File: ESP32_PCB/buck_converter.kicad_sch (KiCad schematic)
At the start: 8 parts, among them U4 TPS54302

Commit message: start pcb
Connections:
- net GNDREF: now also C10.1
- net at C9.1, R7.2, R8.1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: no longer C10.1
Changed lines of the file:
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@@
+		(color 0 0 0 0)
+	)
+	(junction
+		(at 187.96 80.01)
+		(diameter 0)
 		(color 0 0 0 0)
 	)
@@
 	(wire
 		(pts
-			(xy 167.64 66.04) (xy 165.1 66.04)
+			(xy 198.12 72.39) (xy 198.12 80.01)
 		)
 		(stroke
@@
 	(wire
 		(pts
-			(xy 187.96 73.66) (xy 198.12 73.66)
+			(xy 167.64 66.04) (xy 165.1 66.04)
 		)
 		(stroke
@@
 	(wire
 		(pts
-			(xy 198.12 72.39) (xy 198.12 73.66)
+			(xy 198.12 80.01) (xy 187.96 80.01)
 		)
 		(stroke

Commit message: rerouting
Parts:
- C7: value 22uF -> 4.7uF
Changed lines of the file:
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@@
 			)
 		)
-		(property "Value" "22uF"
+		(property "Value" "4.7uF"
 			(at 138.43 59.8169 0)
 			(effects

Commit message: add lcsc pn
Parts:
- removed C7: 4.7uF, Capacitor_SMD:C_0603_1608Metric, symbol Device:C_Small_US
- added C3: 6.8uF, Capacitor_Tantalum_SMD:CP_EIA-3216-18_Kemet-A, symbol Device:C_Polarized_Small_US
- C10: footprint Capacitor_SMD:C_0402_1005Metric -> Capacitor_SMD:C_0805_2012Metric; LCSC PN (none) -> C16780
- C8: LCSC PN (none) -> C14663
- C9: value 56pF -> 82pF; LCSC PN (none) -> C1683
- L1: value 6.8uH -> 10uH; LCSC C207831 -> (none); LCSC PN (none) -> C207831
- R7: footprint Resistor_SMD:R_0603_1608Metric -> Resistor_SMD:R_0805_2012Metric; LCSC PN (none) -> C7319379
- R8: value 22k -> 13.7; footprint Resistor_SMD:R_0603_1608Metric -> Resistor_SMD:R_0805_2012Metric; LCSC PN (none) -> C409962
- U4: footprint Package_TO_SOT_SMD:SOT-23-6 -> Package_TO_SOT_SMD:SOT-563; LCSC PN (none) -> C50310967
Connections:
- net GNDREF: now also C3.2
- net VBATT: now also C3.1
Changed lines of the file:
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@@
+			)
+		)
+		(property "LCSC PN" "C14663"
+			(at 162.56 64.77 90)
+			(effects
+				(font
+					(size 1.27 1.27)
+				)
+				(hide yes)
+			)
+		)
+		(property "LCSC" ""
+			(at 162.56 64.77 90)
+			(effects
+				(font
+					(size 1.27 1.27)
+				)
+				(hide yes)
 			)
 		)
@@
 			)
 		)
-		(property "Footprint" "Package_TO_SOT_SMD:SOT-23-6"
+		(property "Footprint" "Package_TO_SOT_SMD:SOT-563"
 			(at 149.86 76.2 0)
 			(effects
@@
 		)
 		(property "Description" "3A, 4.5 to 28V Input, EMI Friendly integrated switch synchronous step-down regulator, pulse-skipping, SOT-23-6"
+			(at 148.59 67.31 0)
+			(effects
+				(font
+					(size 1.27 1.27)
+				)
+				(hide yes)
+			)
+		)
+		(property "LCSC PN" "C50310967"
+			(at 148.59 67.31 0)
+			(effects
+				(font
+					(size 1.27 1.27)
+				)
+				(hide yes)
+			)
+		)
+		(property "LCSC" ""
 			(at 148.59 67.31 0)
 			(effects
@@
 			)
 		)
-		(property "Footprint" "Capacitor_SMD:C_0402_1005Metric"
+		(property "Footprint" "Capacitor_SMD:C_0805_2012Metric"
 			(at 198.12 69.85 0)
 			(effects
@@
 		)
 		(property "Description" "capacitor, small US symbol"
+			(at 198.12 69.85 0)
+			(effects
+				(font
+					(size 1.27 1.27)
+				)
+				(hide yes)
+			)
+		)
+		(property "LCSC PN" "C16780"
+			(at 198.12 69.85 0)
+			(effects
+				(font
+					(size 1.27 1.27)
+				)
+				(hide yes)
+			)
+		)
+		(property "LCSC" ""
 			(at 198.12 69.85 0)
 			(effects
@@
 	(symbol
 		(lib_id "Device:C_Small_US")
-		(at 135.89 58.42 0)
-		(unit 1)
-		(exclude_from_sim no)
-		(in_bom yes)
-		(on_board yes)
-		(dnp no)
-		(fields_autoplaced yes)
-		(property "Reference" "C7"
-			(at 138.43 57.2769 0)
-			(effects
-				(font
-					(size 1.27 1.27)
-				)
-				(justify left)
-			)
-		)
-		(property "Value" "4.7uF"
-			(at 138.43 59.8169 0)
-			(effects
-				(font
-					(size 1.27 1.27)
-				)
-				(justify left)
-			)
-		)
-		(property "Footprint" "Capacitor_SMD:C_0603_1608Metric"
-			(at 135.89 58.42 0)
-			(effects
-				(font
-					(size 1.27 1.27)
-				)
-				(hide yes)
-			)
-		)
-		(property "Datasheet" ""
-			(at 135.89 58.42 0)
-			(effects
-				(font
-					(size 1.27 1.27)
-				)
-				(hide yes)
-			)
-		)
-		(property "Description" "capacitor, small US symbol"
-			(at 135.89 58.42 0)
-			(effects
-				(font
-					(size 1.27 1.27)
-				)
-				(hide yes)
-			)
-		)
-		(pin "1"
-		)
-		(pin "2"
-		)
-		(instances
-			(project ""
-				(path "/c820eee0-9a51-4601-b23c-3906ac354886/7478e98e-de6a-4a00-aa38-12c004b4cc7e"
-					(reference "C7")
-					(unit 1)
-				)
-			)
-		)
-	)
-	(symbol
-		(lib_id "Device:C_Small_US")
 		(at 177.8 69.85 180)
 		(unit 1)
@@
 			)
 		)
-		(property "Value" "56pF"
+		(property "Value" "82pF"
 			(at 180.34 70.9929 0)
 			(effects
@@
 		)
 		(property "Description" "capacitor, small US symbol"
+			(at 177.8 69.85 0)
+			(effects
+				(font
+					(size 1.27 1.27)
+				)
+				(hide yes)
+			)
+		)
+		(property "LCSC PN" "C1683"
+			(at 177.8 69.85 0)
+			(effects
+				(font
+					(size 1.27 1.27)
+				)
+				(hide yes)
+			)
+		)
+		(property "LCSC" ""
 			(at 177.8 69.85 0)
 			(effects
@@
 			)
 		)
-		(property "Value" "6.8uH"
+		(property "Value" "10uH"
 			(at 171.45 63.5 90)
 			(effects
@@
 			)
 		)
-		(property "LCSC" "C207831"
+		(property "LCSC PN" "C207831"
+			(at 171.45 66.04 90)
+			(effects
+				(font
+					(size 1.27 1.27)
+				)
+				(hide yes)
+			)
+		)
+		(property "LCSC" ""
 			(at 171.45 66.04 90)
 			(effects
@@
 	)
 	(symbol
+		(lib_id "Device:C_Polarized_Small_US")
+		(at 135.89 58.42 0)
+		(mirror x)
+		(unit 1)
+		(exclude_from_sim no)
+		(in_bom yes)
+		(on_board yes)
+		(dnp no)
+		(property "Reference" "C3"
+			(at 138.43 60.1219 0)
+			(effects
+				(font
+					(size 1.27 1.27)
+				)
+				(justify left)
+			)
+		)
+		(property "Value" "6.8uF"
+			(at 138.43 57.5819 0)
+			(effects
+				(font
+					(size 1.27 1.27)
+				)
+				(justify left)
+			)
+		)
+		(property "Footprint" "Capacitor_Tantalum_SMD:CP_EIA-3216-18_Kemet-A"
+			(at 135.89 58.42 0)
+			(effects
+				(font
+					(size 1.27 1.27)
+				)
+				(hide yes)
+			)
+		)
+		(property "Datasheet" "~"
+			(at 135.89 58.42 0)
+			(effects
+				(font
+					(size 1.27 1.27)
+				)
+				(hide yes)
+			)
+		)
+		(property "Description" "Polarized capacitor, small US symbol"
+			(at 135.89 58.42 0)
+			(effects
+				(font
+					(size 1.27 1.27)
+				)
+				(hide yes)
+			)
+		)
+		(property "LCSC PN" "C444749"
+			(at 135.89 58.42 0)
+			(effects
+				(font
+					(size 1.27 1.27)
+				)
+				(hide yes)
+			)
+		)
+		(property "LCSC" ""
+			(at 135.89 58.42 0)
+			(effects
+				(font
+					(size 1.27 1.27)
+				)
+				(hide yes)
+			)
+		)
+		(pin "1"
+		)
+		(pin "2"
+		)
+		(instances
+			(project ""
+				(path "/c820eee0-9a51-4601-b23c-3906ac354886/7478e98e-de6a-4a00-aa38-12c004b4cc7e"
+					(reference "C3")
+					(unit 1)
+				)
+			)
+		)
+	)
+	(symbol
 		(lib_id "Device:R_Small_US")
 		(at 187.96 77.47 0)
@@
 			)
 		)
-		(property "Value" "22k"
+		(property "Value" "13.7"
 			(at 190.5 78.7399 0)
 			(effects
@@
 			)
 		)
-		(property "Footprint" "Resistor_SMD:R_0603_1608Metric"
+		(property "Footprint" "Resistor_SMD:R_0805_2012Metric"
 			(at 187.96 77.47 0)
 			(effects
@@
 		)
 		(property "Description" "Resistor, small US symbol"
+			(at 187.96 77.47 0)
+			(effects
+				(font
+					(size 1.27 1.27)
+				)
+				(hide yes)
+			)
+		)
+		(property "LCSC PN" "C409962"
+			(at 187.96 77.47 0)
+			(effects
+				(font
+					(size 1.27 1.27)
+				)
+				(hide yes)
+			)
+		)
+		(property "LCSC" ""
 			(at 187.96 77.47 0)
 			(effects
@@
 			)
 		)
-		(property "Footprint" "Resistor_SMD:R_0603_1608Metric"
+		(property "Footprint" "Resistor_SMD:R_0805_2012Metric"
 			(at 187.96 69.85 0)
 			(effects
@@
 			(at 187.96 69.85 0)
 			(effects
+				(font
+					(size 1.27 1.27)
+				)
+				(hide yes)
+			)
+		)
+		(property "LCSC PN" "C7319379"
+			(at 187.96 69.85 0)
+			(effects
+				(font
+					(size 1.27 1.27)
+				)
+				(hide yes)
+			)
+		)
+		(property "LCSC" ""
+			(at 187.96 69.85 0)
+			(effects

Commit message: Fix LCSC and PCB
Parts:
- C9: footprint Capacitor_SMD:C_0201_0603Metric -> Capacitor_SMD:C_0603_1608Metric
- L1: footprint Inductor_SMD:L_APV_APH0420 -> Inductor_SMD:L_APV_APH0630; LCSC PN C207831 -> C5349698
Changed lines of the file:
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@@
 			)
 		)
-		(property "Footprint" "Capacitor_SMD:C_0201_0603Metric"
+		(property "Footprint" "Capacitor_SMD:C_0603_1608Metric"
 			(at 177.8 69.85 0)
 			(effects
@@
 			)
 		)
-		(property "Footprint" "Inductor_SMD:L_APV_APH0420"
+		(property "Footprint" "Inductor_SMD:L_APV_APH0630"
 			(at 171.45 66.04 0)
 			(effects
@@
 			)
 		)
-		(property "LCSC PN" "C207831"
+		(property "LCSC PN" "C5349698"
 			(at 171.45 66.04 90)
 			(effects

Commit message: fix U4
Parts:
- U4: footprint Package_TO_SOT_SMD:SOT-563 -> Package_TO_SOT_SMD:TSOT-23-6; LCSC PN C50310967 -> C311983
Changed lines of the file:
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@@
 			)
 		)
-		(property "Footprint" "Package_TO_SOT_SMD:SOT-563"
+		(property "Footprint" "Package_TO_SOT_SMD:TSOT-23-6"
 			(at 149.86 76.2 0)
 			(effects
@@
 			)
 		)
-		(property "Datasheet" "http://www.ti.com/lit/ds/symlink/tps54302.pdf"
+		(property "Datasheet" "https://www.lcsc.com/datasheet/C311983.pdf"
 			(at 140.97 58.42 0)
 			(effects
@@
 			)
 		)
-		(property "Description" "3A, 4.5 to 28V Input, EMI Friendly integrated switch synchronous step-down regulator, pulse-skipping, SOT-23-6"
+		(property "Description" "Buck Switching Regulator IC Adjustable 1 Output 3A TSOT-23-6"
 			(at 148.59 67.31 0)
 			(effects
@@
 			)
 		)
-		(property "LCSC PN" "C50310967"
+		(property "LCSC PN" "C311983"
 			(at 148.59 67.31 0)
 			(effects
-				(font
-					(size 1.27 1.27)
-				)
-				(hide yes)
-			)
-		)
-		(property "LCSC" ""
-			(at 148.59 67.31 0)
-			(effects

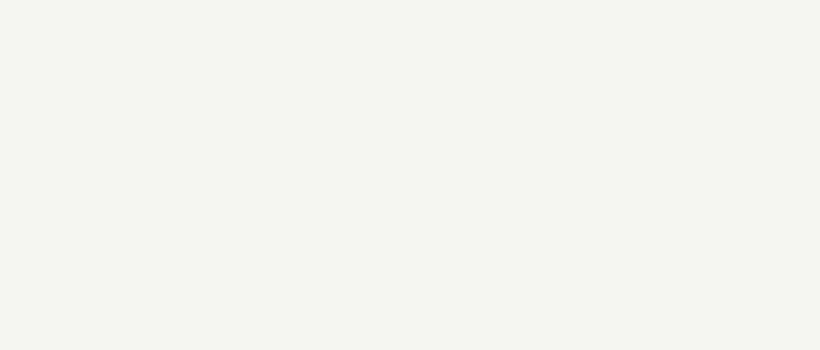
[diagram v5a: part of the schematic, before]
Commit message: add esp32s3 cnofig
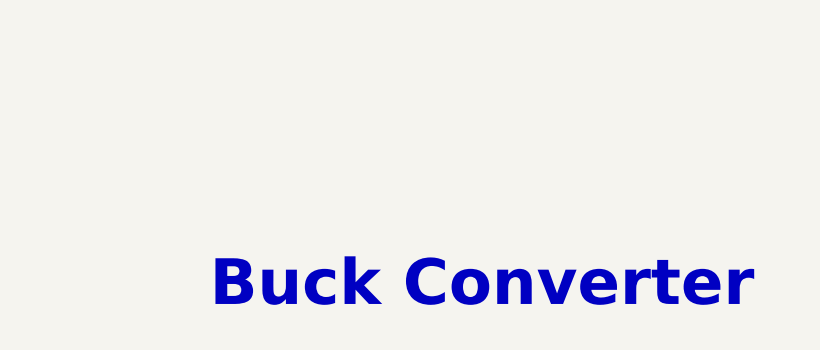
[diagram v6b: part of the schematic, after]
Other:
- note added: "Buck Converter"
- title: (none) -> buck_converter
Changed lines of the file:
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@@
 	(generator_version "9.0")
 	(paper "A4")
+	(title_block
+		(title "buck_converter")
+	)
+	(text "Buck Converter"
+		(exclude_from_sim no)
+		(at 209.042 174.752 0)
+		(effects
+			(font
+				(size 5.08 5.08)
+				(thickness 1.016)
+				(bold yes)
+			)
+		)
+	)
 	(junction
 		(at 187.96 66.04)
